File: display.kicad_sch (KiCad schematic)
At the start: 0 parts

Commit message: add initial display circuit
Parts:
- added J3: Conn_01x02_Pin, symbol Connector:Conn_01x02_Pin
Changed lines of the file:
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@@
 (kicad_sch (version 20230121) (generator eeschema)
   (paper "A4")
+  (symbol (lib_id "Connector:Conn_01x02_Pin") (at 60.706 76.454 0) (unit 1)
+    (in_bom yes) (on_board yes) (dnp no) (fields_autoplaced)
+    (property "Reference" "J3" (at 61.341 71.12 0)
+      (effects (font (size 1.27 1.27)))
+    )
+    (property "Value" "Conn_01x02_Pin" (at 61.341 73.66 0)
+      (effects (font (size 1.27 1.27)))
+    )
+    (property "Footprint" "" (at 60.706 76.454 0)
+      (effects (font (size 1.27 1.27)) hide)
+    )
+    (property "Datasheet" "~" (at 60.706 76.454 0)
+      (effects (font (size 1.27 1.27)) hide)
+    )
+    (pin "1")
+    (pin "2")
+    (instances
+      (project "scale"
+        (path "/8f227bf3-f4cf-485c-a746-8377af835d89/b5072de9-1b37-4196-ac13-e62e0361c228"
+          (reference "J3") (unit 1)
+        )
+      )
+    )
+  )
 )

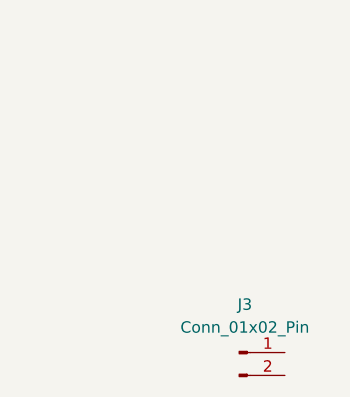
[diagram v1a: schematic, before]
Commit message: add footprint and step
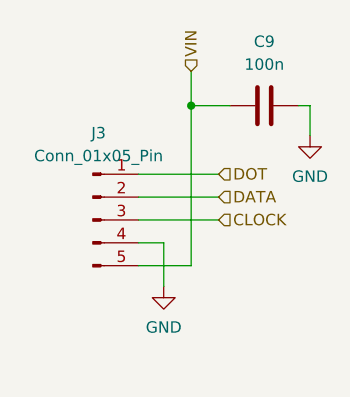
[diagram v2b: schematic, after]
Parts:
- removed J3: Conn_01x02_Pin, symbol Connector:Conn_01x02_Pin
- added C9: 100n, Capacitor_SMD:C_0805_2012Metric, symbol Device:C
- added J3: Conn_01x05_Pin, BBG:JST_S5B-XH-A_LF__SN_, symbol Connector:Conn_01x05_Pin
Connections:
- new net CLOCK: J3.3 (Pin_3)
- new net DATA: J3.2 (Pin_2)
- new net DOT: J3.1 (Pin_1)
- new net GND: C9.2, J3.4 (Pin_4)
- new net VIN: C9.1, J3.5 (Pin_5)
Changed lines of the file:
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@@
 (kicad_sch (version 20230121) (generator eeschema)
   (paper "A4")
-  (symbol (lib_id "Connector:Conn_01x02_Pin") (at 60.706 76.454 0) (unit 1)
+  (junction (at 55.372 49.022) (diameter 0) (color 0 0 0 0)
+  )
+  (wire (pts (xy 49.53 61.722) (xy 58.42 61.722))
+    (stroke (width 0) (type default))
+  )
+  (wire (pts (xy 49.53 56.642) (xy 58.42 56.642))
+    (stroke (width 0) (type default))
+  )
+  (wire (pts (xy 55.372 49.022) (xy 59.69 49.022))
+    (stroke (width 0) (type default))
+  )
+  (wire (pts (xy 49.53 59.182) (xy 58.42 59.182))
+    (stroke (width 0) (type default))
+  )
+  (wire (pts (xy 52.324 64.262) (xy 52.324 69.088))
+    (stroke (width 0) (type default))
+  )
+  (wire (pts (xy 49.53 66.802) (xy 55.372 66.802))
+    (stroke (width 0) (type default))
+  )
+  (wire (pts (xy 49.53 64.262) (xy 52.324 64.262))
+    (stroke (width 0) (type default))
+  )
+  (wire (pts (xy 67.31 49.022) (xy 68.58 49.022))
+    (stroke (width 0) (type default))
+  )
+  (wire (pts (xy 55.372 45.212) (xy 55.372 49.022))
+    (stroke (width 0) (type default))
+  )
+  (wire (pts (xy 55.372 49.022) (xy 55.372 66.802))
+    (stroke (width 0) (type default))
+  )
+  (wire (pts (xy 68.58 49.022) (xy 68.58 52.324))
+    (stroke (width 0) (type default))
+  )
+  (hierarchical_label "VIN" (shape input) (at 55.372 45.212 90) (fields_autoplaced)
+    (effects (font (size 1.27 1.27)) (justify left))
+  )
+  (hierarchical_label "CLOCK" (shape input) (at 58.42 61.722 0) (fields_autoplaced)
+    (effects (font (size 1.27 1.27)) (justify left))
+  )
+  (hierarchical_label "DOT" (shape input) (at 58.42 56.642 0) (fields_autoplaced)
+    (effects (font (size 1.27 1.27)) (justify left))
+  )
+  (hierarchical_label "DATA" (shape input) (at 58.42 59.182 0) (fields_autoplaced)
+    (effects (font (size 1.27 1.27)) (justify left))
+  )
+  (symbol (lib_id "power:GND") (at 52.324 69.088 0) (unit 1)
     (in_bom yes) (on_board yes) (dnp no) (fields_autoplaced)
-    (property "Reference" "J3" (at 61.341 71.12 0)
+    (property "Reference" "#PWR030" (at 52.324 75.438 0)
+      (effects (font (size 1.27 1.27)) hide)
+    )
+    (property "Value" "GND" (at 52.324 73.66 0)
       (effects (font (size 1.27 1.27)))
     )
-    (property "Value" "Conn_01x02_Pin" (at 61.341 73.66 0)
+    (property "Footprint" "" (at 52.324 69.088 0)
+      (effects (font (size 1.27 1.27)) hide)
+    )
+    (property "Datasheet" "" (at 52.324 69.088 0)
+      (effects (font (size 1.27 1.27)) hide)
+    )
+    (pin "1")
+    (instances
+      (project "scale"
+        (path "/8f227bf3-f4cf-485c-a746-8377af835d89/b5072de9-1b37-4196-ac13-e62e0361c228"
+          (reference "#PWR030") (unit 1)
+        )
+      )
+    )
+  )
+  (symbol (lib_id "Device:C") (at 63.5 49.022 90) (unit 1)
+    (in_bom yes) (on_board yes) (dnp no) (fields_autoplaced)
+    (property "Reference" "C9" (at 63.5 41.91 90)
       (effects (font (size 1.27 1.27)))
     )
-    (property "Footprint" "" (at 60.706 76.454 0)
+    (property "Value" "100n" (at 63.5 44.45 90)
+      (effects (font (size 1.27 1.27)))
+    )
+    (property "Footprint" "Capacitor_SMD:C_0805_2012Metric" (at 67.31 48.0568 0)
       (effects (font (size 1.27 1.27)) hide)
     )
-    (property "Datasheet" "~" (at 60.706 76.454 0)
+    (property "Datasheet" "~" (at 63.5 49.022 0)
       (effects (font (size 1.27 1.27)) hide)
     )
@@
       (project "scale"
         (path "/8f227bf3-f4cf-485c-a746-8377af835d89/b5072de9-1b37-4196-ac13-e62e0361c228"
+          (reference "C9") (unit 1)
+        )
+      )
+    )
+  )
+  (symbol (lib_id "Connector:Conn_01x05_Pin") (at 44.45 61.722 0) (unit 1)
+    (in_bom yes) (on_board yes) (dnp no) (fields_autoplaced)
+    (property "Reference" "J3" (at 45.085 52.07 0)
+      (effects (font (size 1.27 1.27)))
+    )
+    (property "Value" "Conn_01x05_Pin" (at 45.085 54.61 0)
+      (effects (font (size 1.27 1.27)))
+    )
+    (property "Footprint" "BBG:JST_S5B-XH-A_LF__SN_" (at 44.45 61.722 0)
+      (effects (font (size 1.27 1.27)) hide)
+    )
+    (property "Datasheet" "~" (at 44.45 61.722 0)
+      (effects (font (size 1.27 1.27)) hide)
+    )
+    (pin "5")
+    (pin "2")
+    (pin "4")
+    (pin "3")
+    (pin "1")
+    (instances
+      (project "scale"
+        (path "/8f227bf3-f4cf-485c-a746-8377af835d89/b5072de9-1b37-4196-ac13-e62e0361c228"
           (reference "J3") (unit 1)
         )
       )
+    )
+  )
+  (symbol (lib_id "power:GND") (at 68.58 52.324 0) (unit 1)
+    (in_bom yes) (on_board yes) (dnp no) (fields_autoplaced)
+    (property "Reference" "#PWR032" (at 68.58 58.674 0)
+      (effects (font (size 1.27 1.27)) hide)
+    )
+    (property "Value" "GND" (at 68.58 56.896 0)
+      (effects (font (size 1.27 1.27)))
+    )
+    (property "Footprint" "" (at 68.58 52.324 0)
+      (effects (font (size 1.27 1.27)) hide)
+    )
+    (property "Datasheet" "" (at 68.58 52.324 0)
+      (effects (font (size 1.27 1.27)) hide)
+    )
+    (pin "1")
+    (instances
+      (project "scale"
+        (path "/8f227bf3-f4cf-485c-a746-8377af835d89/b5072de9-1b37-4196-ac13-e62e0361c228"
+          (reference "#PWR032") (unit 1)
+        )
+      )
